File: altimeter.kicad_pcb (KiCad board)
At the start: 4 copper layers, 45 x 24 mm, 86 parts, among them J201 Conn_01x10, J202 Conn_ARM_JTAG_SWD_10, J203 Conn_02x03_Counter_Clockwise, J204 USB_B_Micro, J205 Conn_01x04, Q1 BC848CDW1T1G, Q101 DMG2301L, Q102 NTR4003NT1G, Q103 SISS05dn, Q301 BC848CDW1T1G, Q401 BC848CDW1T1G, Q501 BC848CDW1T1G, U1 LMV331, U101 STM32F303CCTx, U102 S25FL512SAGMFIR11, U103 AIS2120SXTR, U104 MIC5219-3.3YM5, U105 LF50_TO252, U106 BMI088, U107 MS5611-01BA, U201 USBLC6-2SC6, U301 SI7232DN, U501 SI7232DN, Y1 Crystal_GND24

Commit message: fix wrong connection of quarz
Signed-off-by: Thomas Schmid <tom@binary-kitchen.de>
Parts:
- added R106: 2.7k, Resistor_SMD:R_0402_1005Metric, F.Cu at (178.5, 104.9)
- moved Y1 0.55 mm to (151.9, 116.4)
- moved C101 0.36 mm to (153.9, 117.3)
- moved C102 0.27 mm to (153.9, 115.6)
- moved C114 0.07 mm to (153.5, 113.3)
- moved C112 0.06 mm to (153.5, 114.2)
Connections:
- U101 pad 3: Net-(U101-Pad3) -> INT2
- U101 pad 38: INT1 -> LED1
- U101 pad 4: Net-(C102-Pad1) -> INT1
- U101 pad 5: LED1 -> Net-(C101-Pad1)
- U101 pad 6: INT2 -> Net-(C102-Pad1)
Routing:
- net LED1: track 7.86 -> 12.9 mm, vias 1 -> 3
- net SUMMER: track 19.3 -> 24.1 mm, vias 1 -> 2
- net INT1: track 17.9 -> 20.8 mm
- net GND: track 128.6 -> 129.8 mm
- net Net-(C101-Pad1): track 4.64 -> 5.52 mm
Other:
- board text added: "V1.1 rev.A"
- board text removed: "JLCJLCJLCJLC"
- board text removed: "V1.0 rev.B"

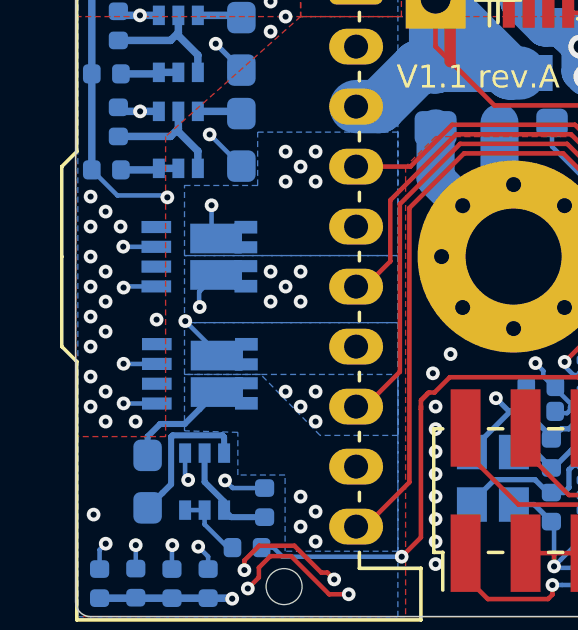
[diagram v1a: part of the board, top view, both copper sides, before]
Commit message: fix swaped gate and source pin of pyro mosfets
Signed-off-by: Thomas Schmid <tom@binary-kitchen.de>
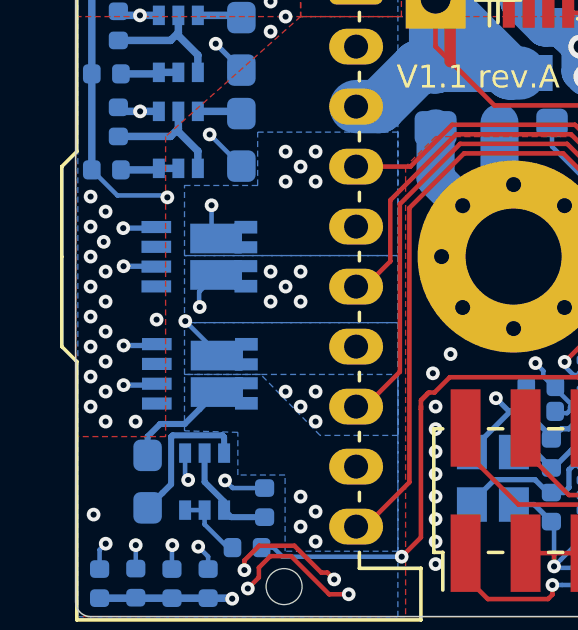
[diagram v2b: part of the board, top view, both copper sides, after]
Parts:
- U201: value USBLC6-2SC6 -> USBLC6-2P6
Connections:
- J202 pad 7: Net-(J202-Pad7) -> (no net)
- J202 pad 8: Net-(J202-Pad8) -> (no net)
- J204 pad 4: Net-(J204-Pad4) -> (no net)
- U101 pad 20: IMU_GYRO_CS -> IMU_ACC_CS
- U101 pad 21: IMU_ACC_CS -> IMU_GYRO_CS
- U102 pad 11: Net-(U102-Pad11) -> (no net)
- U102 pad 12: Net-(U102-Pad12) -> (no net)
- U102 pad 13: Net-(U102-Pad13) -> (no net)
- U102 pad 14: Net-(U102-Pad14) -> (no net)
- U102 pad 4: Net-(U102-Pad4) -> (no net)
- U102 pad 5: Net-(U102-Pad5) -> (no net)
- U102 pad 6: Net-(U102-Pad6) -> (no net)
- U106 pad 1: Net-(U106-Pad1) -> (no net)
- U106 pad 13: Net-(U106-Pad13) -> (no net)
- U106 pad 14: IMU_GYRO_CS -> IMU_ACC_CS
- U106 pad 5: IMU_ACC_CS -> IMU_GYRO_CS
- U301 pad 1: FIRE_PYRO1 -> GND
- U301 pad 2: GND -> FIRE_PYRO1
- U301 pad 3: FIRE_PYRO0 -> GND
- U301 pad 4: GND -> FIRE_PYRO0
- U501 pad 1: FIRE_PYRO3 -> GND
- U501 pad 2: GND -> FIRE_PYRO3
- U501 pad 3: FIRE_PYRO2 -> GND
- U501 pad 4: GND -> FIRE_PYRO2
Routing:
- net IMU_GYRO_CS: track 12.3 -> 15.0 mm, vias 2 -> 0
- net IMU_ACC_CS: track 15.0 -> 12.3 mm, vias 0 -> 2
- net FIRE_PYRO3: track 28.4 -> 29.0 mm
- net GND: vias 64 -> 65

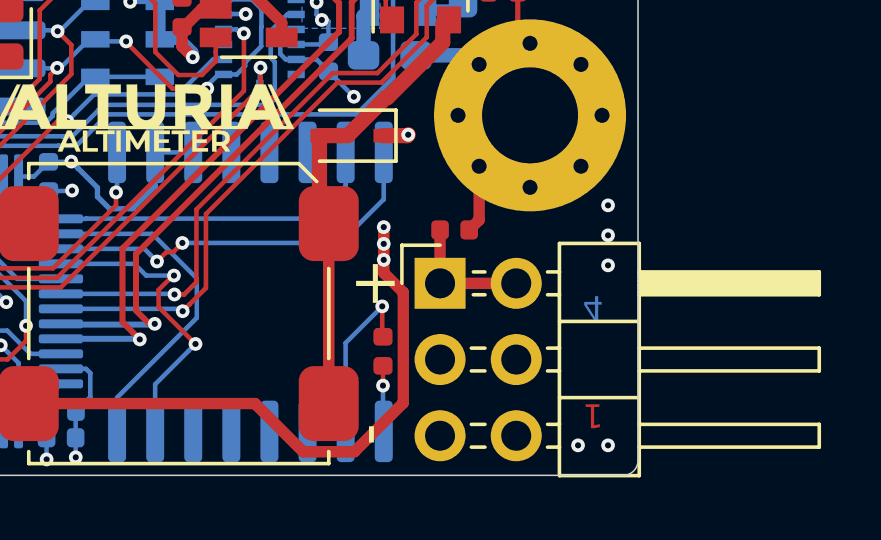
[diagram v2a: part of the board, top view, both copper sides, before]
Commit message: fix servo connectors
fix pinout of servo connectors. 5V Pin and Signal was swapped

Signed-off-by: Thomas Schmid <tom@binary-kitchen.de>
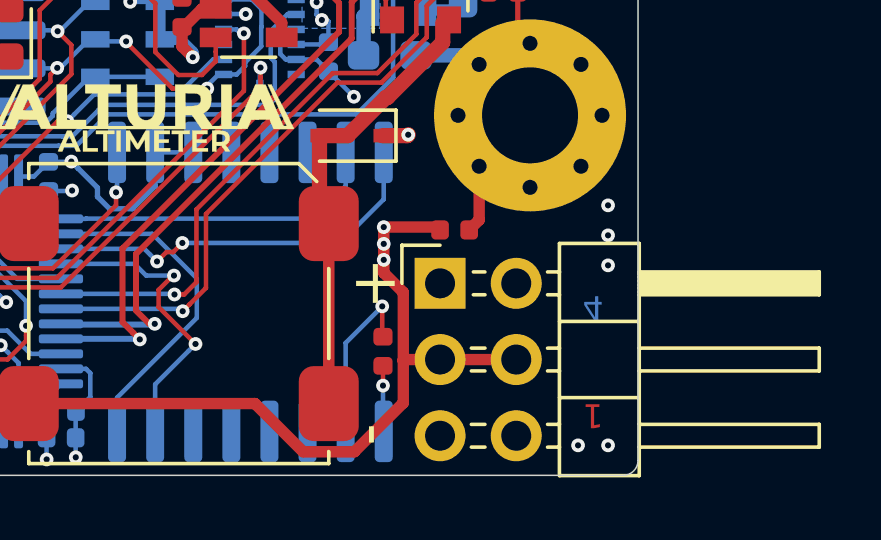
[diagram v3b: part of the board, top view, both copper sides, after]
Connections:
- J203 pad 1: +5V -> PWM2
- J203 pad 2: +5V -> PWM1
- J203 pad 3: PWM1 -> +5V
- J203 pad 4: PWM2 -> +5V
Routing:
- net PWM1: track 21.8 -> 25.4 mm
- net PWM2: track 25.8 -> 23.3 mm
- net +5V: track 61.3 -> 62.7 mm

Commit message: v1.2 rev A
Signed-off-by: Thomas Schmid <tom@binary-kitchen.de>
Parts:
- removed C105: 470p, Capacitor_SMD:C_0603_1608Metric_Pad1.05x0.95mm_HandSolder
- removed D102: LED, LED_SMD:LED_0603_1608Metric
- removed the Ref** at (166.5, 109.1)
- removed U104: MIC5219-3.3YM5, Package_TO_SOT_SMD:SOT-23-5
- added C117: 2.2u, Capacitor_SMD:C_0402_1005Metric, B.Cu at (174.7, 104.4)
- added C118: 2.2u, Capacitor_SMD:C_0402_1005Metric, B.Cu at (163.5, 104.3)
- added C119: 1u, Capacitor_SMD:C_0805_2012Metric, F.Cu at (158.5, 99.9)
- added C120: 4.7u, Capacitor_SMD:C_0805_2012Metric_Pad1.15x1.40mm_HandSolder, B.Cu at (150.1, 104.1)
- added C121: 4.7u, Capacitor_SMD:C_0805_2012Metric_Pad1.15x1.40mm_HandSolder, F.Cu at (149.9, 103.9)
- added C122: 4.7u, Capacitor_SMD:C_0805_2012Metric_Pad1.15x1.40mm_HandSolder, F.Cu at (153.5, 103.9)
- added C123: 4.7u, Capacitor_SMD:C_0805_2012Metric_Pad1.15x1.40mm_HandSolder, F.Cu at (151.7, 103.9)
- added C124: 4.7u, Capacitor_SMD:C_0603_1608Metric_Pad1.05x0.95mm_HandSolder, F.Cu at (158.1, 105.3)
- added C204: 100n, Capacitor_SMD:C_0402_1005Metric, F.Cu at (163.2, 101.8)
- added C205: 100n, Capacitor_SMD:C_0402_1005Metric, B.Cu at (168.6, 103.0)
- added J206: Conn_01x10_MountingPin, Connector_Molex:Molex_PicoBlade_53398-1071_1x10-1MP_P1.25mm_Vertical, F.Cu at (166.1, 107.4)
- added R107: 680, Resistor_SMD:R_0402_1005Metric, F.Cu at (160.3, 110.9)
- added R108: 2.7k, Resistor_SMD:R_0402_1005Metric, B.Cu at (176.6, 112.3)
- added R109: 680, Resistor_SMD:R_0402_1005Metric, B.Cu at (170.5, 118.7)
- added R202: 120, Resistor_SMD:R_0603_1608Metric_Pad1.05x0.95mm_HandSolder, F.Cu at (163.6, 104.7)
- added U108: STM32F405RGTx, Package_QFP:LQFP-64_10x10mm_P0.5mm, B.Cu at (168.7, 110.7)
- added U202: ATA6561, Package_DFN_QFN:DFN-8-1EP_3x3mm_P0.65mm_EP1.55x2.4mm, F.Cu at (167.2, 103.3)
- C1, C106, R1, R11, R2, R3, R4, R5, R6, R7, R8, R9, U201: moved to B.Cu
- C101, C102: value 22p -> 20p
- C104: value 100n -> 4.7u
- C107: value 2.2u -> 4.7u; footprint Capacitor_SMD:C_0603_1608Metric_Pad1.05x0.95mm_HandSolder -> Capacitor_SMD:C_0805_2012Metric
- C108: value 4.7u -> 2.2u; moved to F.Cu
- D101: value LED -> LED_RGBA; footprint LED_SMD:LED_0603_1608Metric -> altimeter:SMD_RGB_LED
- Q101: moved to F.Cu
- U1: footprint Package_TO_SOT_SMD:SOT-23-5 -> Package_TO_SOT_SMD:SOT-353_SC-70-5
- U101: value STM32F303CCTx -> TLV767; footprint Package_QFP:LQFP-48_7x7mm_P0.5mm -> altimeter:TI_WSON_TLV767; moved to F.Cu
- U102: value S25FL512SAGMFIR11 -> MT25Q_W9; footprint Package_SO:SOIC-16W_7.5x10.3mm_P1.27mm -> altimeter:micron-wpdfn_8x6mm
- U105: value LF50_TO252 -> LDL212; footprint Package_TO_SOT_SMD:TO-252-2 -> Package_DFN_QFN:DFN-6-1EP_3x3mm_P0.95mm_EP1.7x2.6mm
- Y1: footprint Crystal:Crystal_SMD_2520-4Pin_2.5x2.0mm -> Crystal:Crystal_SMD_2016-4Pin_2.0x1.6mm
- moved C112 22.5 mm to (173.8, 104.4), turned to 90 degrees
- moved Y1 22.2 mm to (174.0, 119.2), turned to 270 degrees
- moved C114 21.0 mm to (174.4, 115.6), turned to 270 degrees
- moved R2 20.1 mm to (169.8, 120.1)
- moved C113 18.8 mm to (173.9, 116.9), turned to 0 degrees
- moved C102 18.7 mm to (172.0, 119.9)
- moved C101 18.2 mm to (172.0, 118.2), turned to 180 degrees
- moved Ref** 17.6 mm to (174.9, 103.7)
- moved R1 16.9 mm to (169.4, 118.2), turned to 270 degrees
- moved C108 16.9 mm to (158.1, 104.2)
- moved R11 15.8 mm to (168.4, 119.6), turned to 90 degrees
- moved U102 15.8 mm to (154.3, 115.8), turned to 0 degrees
- moved C109 15.7 mm to (156.7, 108.9), turned to 90 degrees
- moved C1 15.4 mm to (159.1, 118.2), turned to 90 degrees
- moved R8 14.7 mm to (165.1, 119.6), turned to 90 degrees
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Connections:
- net Net-(J204-Pad2) renamed /Connectors/USB_D_RAW_N
- net Net-(J204-Pad3) renamed /Connectors/USB_D_RAW_P
- C101 pad 1: Net-(C101-Pad1) -> /OSC_IN
- D101 pad 1: GND -> Net-(D101-Pad1)
- R101 pad 1: Net-(D101-Pad2) -> LED_B
- R101 pad 2: LED1 -> Net-(D101-Pad3)
- R105 pad 1: Net-(D102-Pad2) -> LED_G
- R105 pad 2: +3V3 -> Net-(D101-Pad2)
- U101 pad 2: FLASH_HOLD -> +3V3
- U101 pad 3: INT2 -> GND
- U101 pad 4: INT1 -> +5V
- U101 pad 5: Net-(C101-Pad1) -> GND
- U101 pad 6: Net-(C102-Pad1) -> +5V
- U101 pad 7: NRST -> GND
- U102 pad 1: FLASH_HOLD -> CS_FLASH
- U102 pad 2: +3V3 -> SPI1_MISO
- U102 pad 4: (no net) -> GND
- U102 pad 5: (no net) -> SPI1_MOSI
- U102 pad 6: (no net) -> SPI1_SCK
- U102 pad 7: SPI2_NSS -> FLASH_HOLD
- U102 pad 8: SPI2_MISO -> +3V3
- U102 pad 9: +3V3 -> GND
- U103 pad 1: SPI1_SCK -> SPI2_SCK
- U103 pad 2: SPI1_MOSI -> SPI2_MOSI
- U103 pad 3: SPI1_MISO -> SPI2_MISO
- U105 pad 1: PYRO0_HIGH -> GND
- U105 pad 2: GND -> +5V
- U106 pad 10: SPI1_MISO -> SPI2_MISO
- U106 pad 15: SPI1_MISO -> SPI2_MISO
- U106 pad 8: SPI1_SCK -> SPI2_SCK
- U106 pad 9: SPI1_MOSI -> SPI2_MOSI
- U107 pad 6: SPI1_MISO -> SPI2_MISO
- U107 pad 7: SPI1_MOSI -> SPI2_MOSI
- U107 pad 8: SPI1_SCK -> SPI2_SCK
- Y1 pad 1: Net-(C101-Pad1) -> /OSC_IN
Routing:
- net GND: track 129.8 -> 175.3 mm, vias 65 -> 72
- net +3V3: track 55.9 -> 80.4 mm, vias 13 -> 29
- net PWM2: track 23.3 -> 2.53 mm, vias 1 -> 0
- net PYRO0_HIGH: track 36.8 -> 57.4 mm, vias 0 -> 1
- net PWM1: track 25.4 -> 5.27 mm, vias 1 -> 0
- net PYRO0_LOW: track 24.0 -> 43.4 mm
- net CS_FLASH: track 0.00 -> 19.0 mm
- net SWDIO: track 15.2 -> 34.1 mm, vias 1 -> 3
- net CAN_RX: track 0.00 -> 17.9 mm, vias 0 -> 1
- net CAN_TX: track 0.00 -> 17.7 mm, vias 0 -> 1
- net INT1: track 20.8 -> 4.33 mm, vias 2 -> 0
- net SWCLK: track 12.7 -> 28.7 mm
- net SPI1_SCK: track 21.9 -> 6.65 mm, vias 2 -> 0
- net FIRE_PYRO2: track 34.0 -> 49.2 mm, vias 3 -> 4
- net SWO: track 10.9 -> 25.6 mm
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- added copper zone on F.Cu, net +3V3
- added copper zone on F.Cu, net +5V
- added copper zone on B.Cu, net PYRO0_HIGH
- removed copper zone on B.Cu, net +3V3
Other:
- rule pad_to_mask_clearance: 0.0254 -> 0.05
- rule trace_min: 0.152 -> 0.1524
- board text added: "Alturia Altimeter CC-BY-NC-SA 4.0 T. Schmid © 2020"
- board text added: "JLCJLCJLC"
- board text added: "V1.2 rev.A"
- board text removed: "Alturia Altimeter CC-BY-NC-SA 4.0 T. Schmid © 2019"
- board text removed: "V1.1 rev.A"
